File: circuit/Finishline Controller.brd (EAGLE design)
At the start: 101.6 x 53.3 mm, 20 parts, among them IC1 74HCT245N, IC2 MAX3490ESA

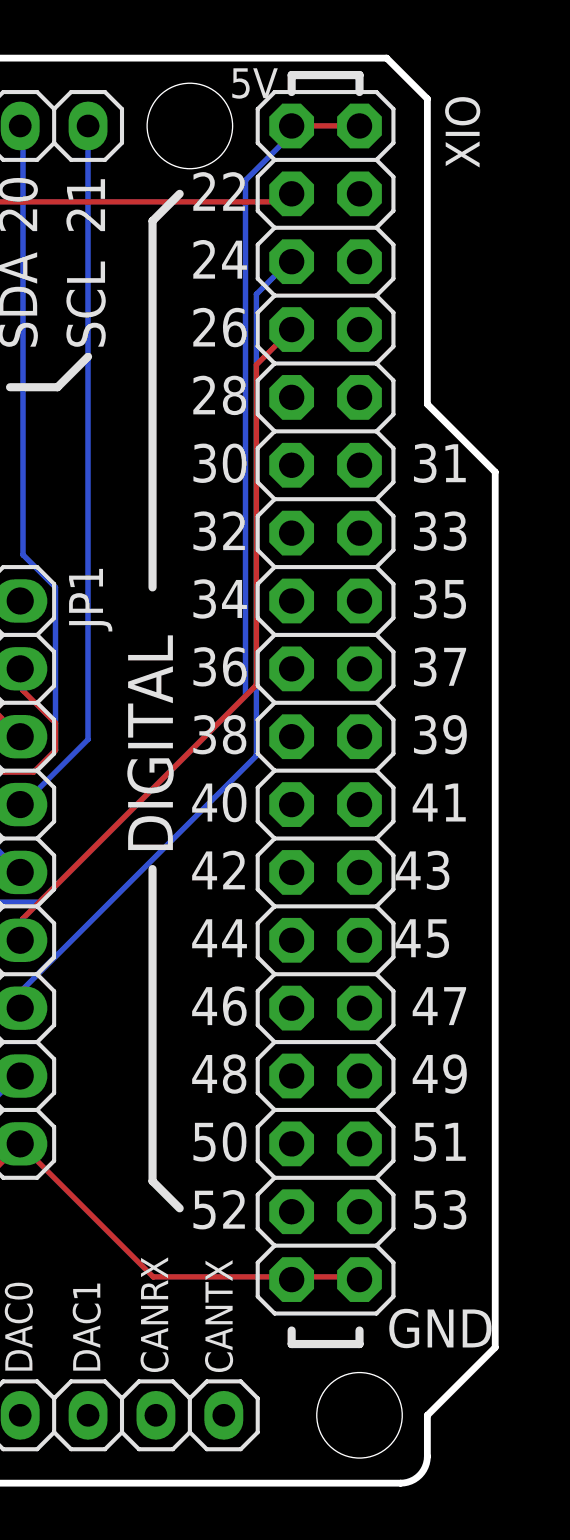
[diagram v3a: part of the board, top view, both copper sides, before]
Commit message: reduce the PCB size of the controller shield to max. 10cm
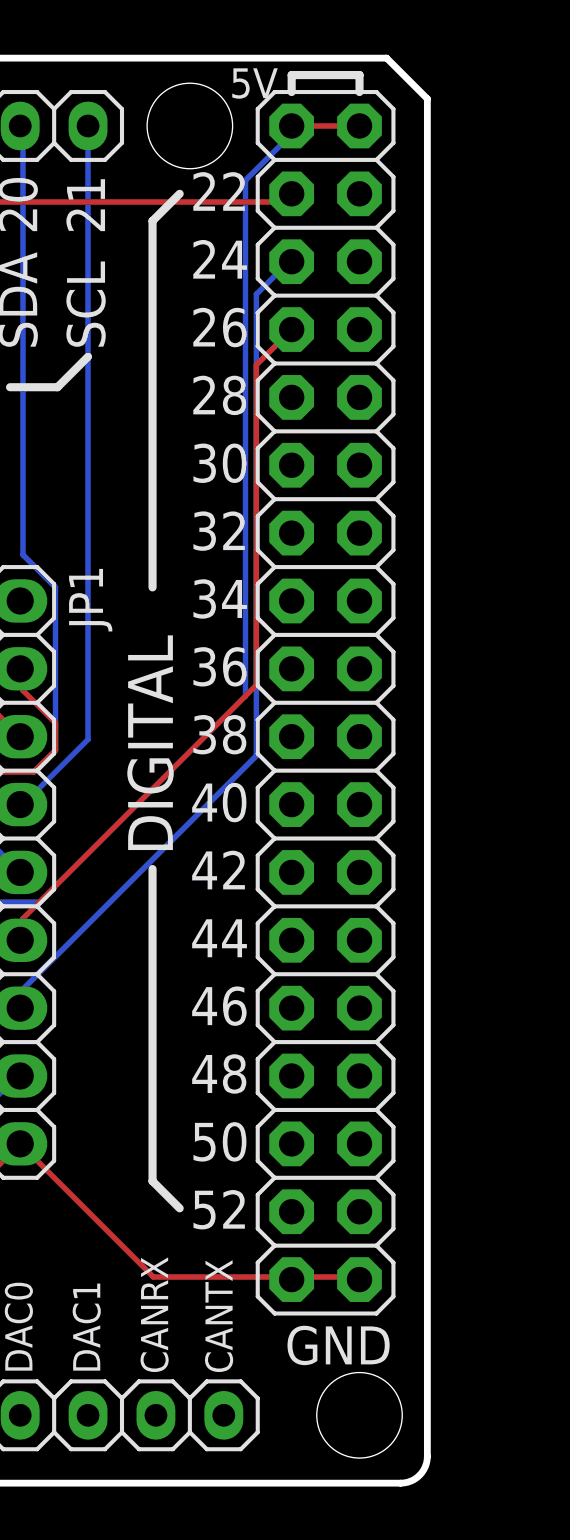
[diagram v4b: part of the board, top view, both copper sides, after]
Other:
- board size 101.6 x 53.3 mm -> 99.1 x 53.3 mm
- board text removed: "31"
- board text removed: "33"
- board text removed: "35"
- board text removed: "37"
- board text removed: "39"
- board text removed: "41"
- board text removed: "43"
- board text removed: "45"
- board text removed: "47"
- board text removed: "49"
- board text removed: "51"
- board text removed: "53"
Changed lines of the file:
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@@
 <setting verticaltext="up"/>
 </settings>
-<grid distance="0.05" unitdist="inch" unit="inch" style="lines" multiple="1" display="yes" altdistance="0.025" altunitdist="inch" altunit="inch"/>
+<grid distance="0.05" unitdist="inch" unit="mm" style="lines" multiple="1" display="yes" altdistance="0.025" altunitdist="inch" altunit="mm"/>
 <layers>
 <layer number="1" name="Top" color="4" fill="1" visible="yes" active="yes"/>
@@
 <layer number="29" name="tStop" color="2" fill="3" visible="yes" active="yes"/>
 <layer number="30" name="bStop" color="5" fill="6" visible="yes" active="yes"/>
-<layer number="31" name="tCream" color="7" fill="4" visible="yes" active="yes"/>
-<layer number="32" name="bCream" color="7" fill="5" visible="yes" active="yes"/>
-<layer number="33" name="tFinish" color="6" fill="3" visible="yes" active="yes"/>
-<layer number="34" name="bFinish" color="6" fill="6" visible="yes" active="yes"/>
+<layer number="31" name="tCream" color="7" fill="4" visible="no" active="yes"/>
+<layer number="32" name="bCream" color="7" fill="5" visible="no" active="yes"/>
+<layer number="33" name="tFinish" color="6" fill="3" visible="no" active="yes"/>
+<layer number="34" name="bFinish" color="6" fill="6" visible="no" active="yes"/>
 <layer number="35" name="tGlue" color="7" fill="4" visible="no" active="yes"/>
 <layer number="36" name="bGlue" color="7" fill="5" visible="no" active="yes"/>
@@
 <layer number="44" name="Drills" color="7" fill="1" visible="yes" active="yes"/>
 <layer number="45" name="Holes" color="7" fill="1" visible="yes" active="yes"/>
-<layer number="46" name="Milling" color="3" fill="1" visible="no" active="yes"/>
-<layer number="47" name="Measures" color="7" fill="1" visible="no" active="yes"/>
-<layer number="48" name="Document" color="7" fill="1" visible="no" active="yes"/>
+<layer number="46" name="Milling" color="3" fill="1" visible="yes" active="yes"/>
+<layer number="47" name="Measures" color="7" fill="1" visible="yes" active="yes"/>
+<layer number="48" name="Document" color="7" fill="1" visible="yes" active="yes"/>
 <layer number="49" name="ReferenceLC" color="13" fill="1" visible="yes" active="yes"/>
 <layer number="50" name="ReferenceLS" color="12" fill="1" visible="yes" active="yes"/>
@@
 <plain>
 <wire x1="97.536" y1="53.34" x2="99.06" y2="51.816" width="0.254" layer="20"/>
-<wire x1="99.06" y1="40.386" x2="101.6" y2="37.846" width="0.254" layer="20"/>
-<wire x1="101.6" y1="37.846" x2="101.6" y2="5.08" width="0.254" layer="20"/>
-<wire x1="101.6" y1="5.08" x2="99.06" y2="2.54" width="0.254" layer="20"/>
-<wire x1="99.06" y1="2.54" x2="99.06" y2="1" width="0.254" layer="20"/>
 <wire x1="99.06" y1="1" x2="98.06" y2="0" width="0.254" layer="20" curve="-90"/>
 <wire x1="98.06" y1="0" x2="1" y2="0" width="0.254" layer="20"/>
@@
 <wire x1="0" y1="52.34" x2="1" y2="53.34" width="0.254" layer="20" curve="-90"/>
 <wire x1="1" y1="53.34" x2="97.536" y2="53.34" width="0.254" layer="20"/>
-<wire x1="99.06" y1="51.816" x2="99.06" y2="40.386" width="0.254" layer="20"/>
-<wire x1="93.98" y1="5.715" x2="93.98" y2="5.207" width="0.3048" layer="21"/>
-<wire x1="93.98" y1="5.207" x2="96.52" y2="5.207" width="0.3048" layer="21"/>
-<wire x1="96.52" y1="5.207" x2="96.52" y2="5.715" width="0.3048" layer="21"/>
+<wire x1="99.06" y1="51.816" x2="99.06" y2="1" width="0.254" layer="20"/>
 <wire x1="93.98" y1="52.07" x2="93.98" y2="52.705" width="0.3048" layer="21"/>
 <wire x1="93.98" y1="52.705" x2="96.52" y2="52.705" width="0.3048" layer="21"/>
@@
 <text x="86.995" y="46.736" size="1.4224" layer="21" font="vector" ratio="12" rot="R90">21</text>
 <text x="93.472" y="52.959" size="1.1176" layer="25" font="vector" ratio="20" rot="R180">5V</text>
-<text x="97.536" y="5.08" size="1.4224" layer="25" font="vector" ratio="12">GND</text>
+<text x="93.726" y="4.445" size="1.4224" layer="25" font="vector" ratio="12">GND</text>
 <text x="90.17" y="47.625" size="1.4224" layer="21" font="vector" ratio="12">22</text>
 <text x="90.17" y="45.085" size="1.4224" layer="21" font="vector" ratio="12">24</text>
@@
 <text x="90.17" y="40.005" size="1.4224" layer="21" font="vector" ratio="12">28</text>
 <text x="90.17" y="37.465" size="1.4224" layer="21" font="vector" ratio="12">30</text>
-<text x="98.425" y="37.465" size="1.4224" layer="21" font="vector" ratio="12">31</text>
 <text x="90.17" y="34.925" size="1.4224" layer="21" font="vector" ratio="12">32</text>
-<text x="98.425" y="34.925" size="1.4224" layer="21" font="vector" ratio="12">33</text>
 <text x="90.17" y="32.385" size="1.4224" layer="21" font="vector" ratio="12">34</text>
-<text x="98.425" y="32.385" size="1.4224" layer="21" font="vector" ratio="12">35</text>
 <text x="90.17" y="29.845" size="1.4224" layer="21" font="vector" ratio="12">36</text>
-<text x="98.425" y="29.845" size="1.4224" layer="21" font="vector" ratio="12">37</text>
 <text x="90.17" y="27.305" size="1.4224" layer="21" font="vector" ratio="12">38</text>
-<text x="98.425" y="27.305" size="1.4224" layer="21" font="vector" ratio="12">39</text>
-<text x="98.425" y="24.765" size="1.4224" layer="21" font="vector" ratio="12">41</text>
 <text x="90.17" y="24.765" size="1.4224" layer="21" font="vector" ratio="12">40</text>
-<text x="97.79" y="22.225" size="1.4224" layer="21" font="vector" ratio="12">43</text>
 <text x="90.17" y="22.225" size="1.4224" layer="21" font="vector" ratio="12">42</text>
-<text x="97.79" y="19.685" size="1.4224" layer="21" font="vector" ratio="12">45</text>
-<text x="98.425" y="17.145" size="1.4224" layer="21" font="vector" ratio="12">47</text>
-<text x="98.425" y="14.605" size="1.4224" layer="21" font="vector" ratio="12">49</text>
-<text x="98.425" y="12.065" size="1.4224" layer="21" font="vector" ratio="12">51</text>
 <text x="90.17" y="19.685" size="1.4224" layer="21" font="vector" ratio="12">44</text>
 <text x="90.17" y="17.145" size="1.4224" layer="21" font="vector" ratio="12">46</text>
 <text x="90.17" y="12.065" size="1.4224" layer="21" font="vector" ratio="12">50</text>
 <text x="90.17" y="14.605" size="1.4224" layer="21" font="vector" ratio="12">48</text>
-<text x="98.425" y="9.525" size="1.4224" layer="21" font="vector" ratio="12">53</text>
 <text x="90.17" y="9.525" size="1.4224" layer="21" font="vector" ratio="12">52</text>
 <text x="89.535" y="23.495" size="1.6764" layer="25" font="vector" ratio="15" rot="R90">DIGITAL</text>
@@
 </element>
 <element name="XIO" library="SmartPrj" package="2X18" value="18x2F-H8.5" x="95.25" y="29.21" locked="yes" smashed="yes" rot="R270">
-<attribute name="NAME" x="99.7458" y="51.9684" size="1.27" layer="25" ratio="10" rot="R270"/>
 <attribute name="VALUE" x="90.805" y="52.07" size="1.27" layer="27" rot="R270"/>
 </element>

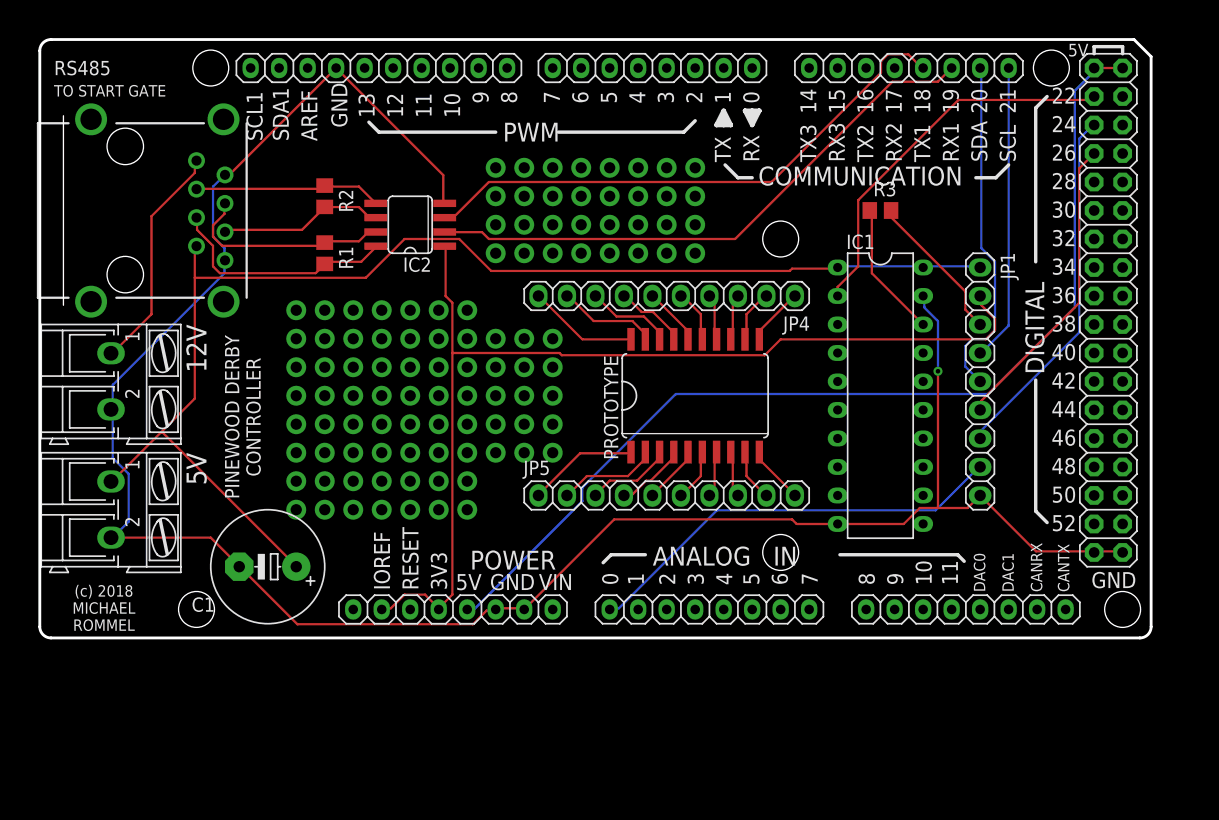
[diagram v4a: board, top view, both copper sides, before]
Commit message: change the pin assignment for LDR and WS2812DATA
This uses a high power pin for the LED data and a normal analog pin for
the LDR line.
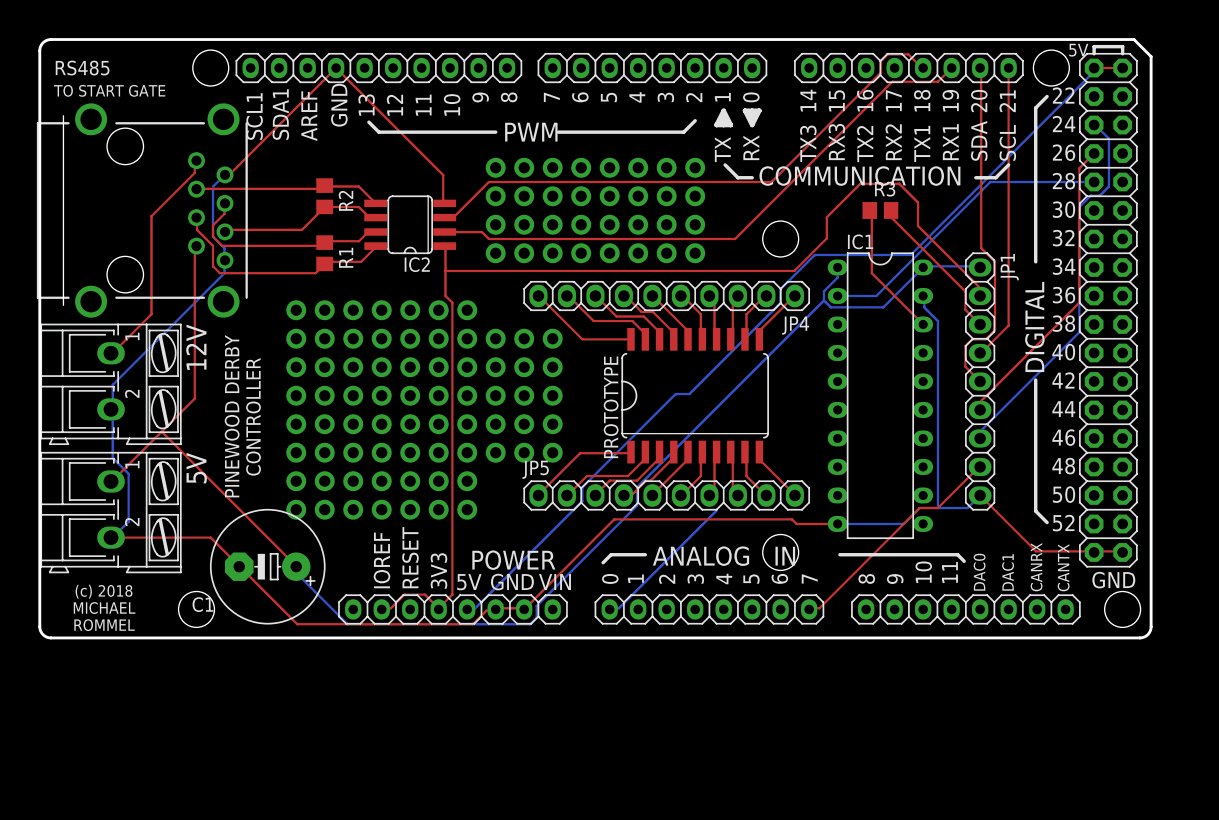
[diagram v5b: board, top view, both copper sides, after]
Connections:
- net AD0: no longer JP1.8
- net AD7: now also JP1.8
- net PIN22: no longer IC1.2
- net PIN28: now also IC1.2
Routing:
- net PIN22: track 34.2 -> 0.00 mm
- net PIN28: track 0.00 -> 27.1 mm
- net AD0: track 38.3 -> 13.3 mm
- net AD7: track 0.00 -> 20.6 mm
- net +5V: track 90.7 -> 80.1 mm
- net +5VEXT: track 114.2 -> 123.4 mm
- net +3.3V: track 92.4 -> 97.2 mm
- net PIN24: track 32.2 -> 33.8 mm
- net GND: vias 1 -> 0

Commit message: correct some schematics mistakes and add gerber files
A demo mode button was added to the controller, the layout of the
controller shield as well as the startgate displays were changed.
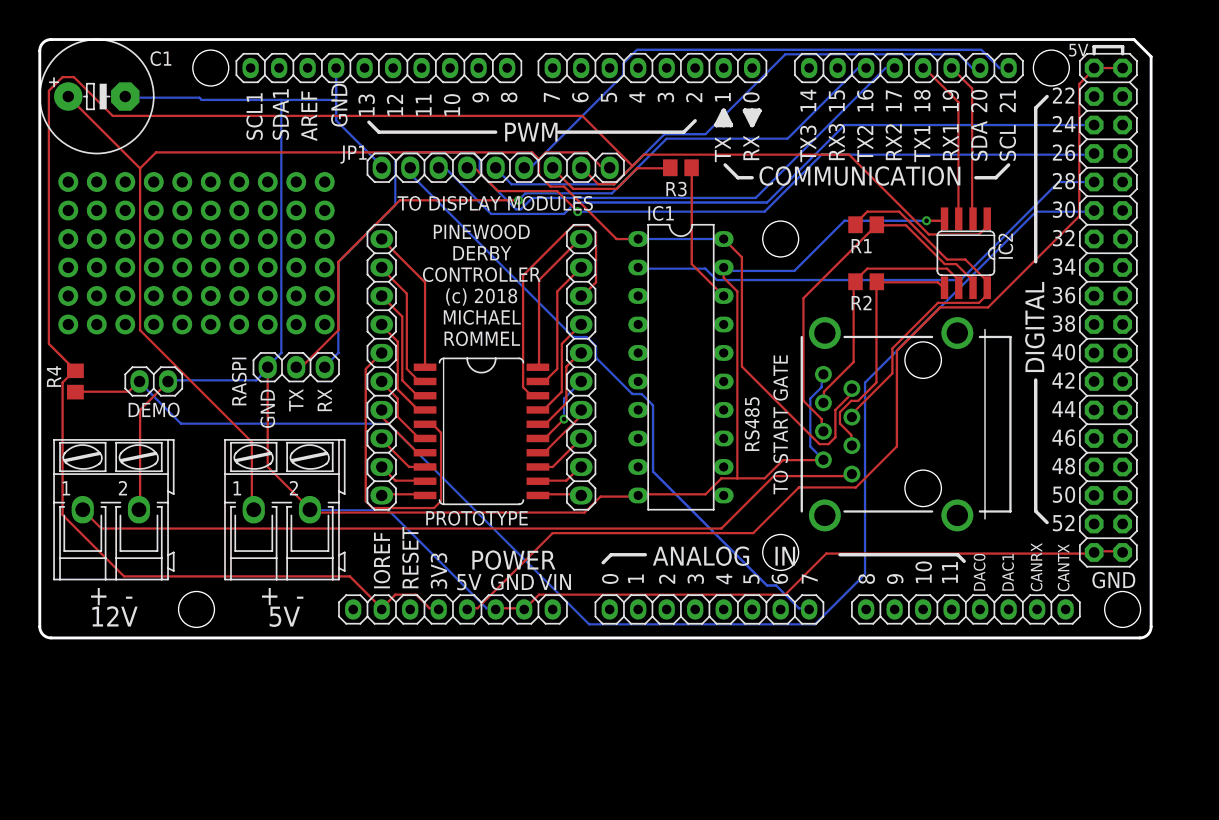
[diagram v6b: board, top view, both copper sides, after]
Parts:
- added JP2: DEMO, pinhead:1X02
- added JP3: RASPI, pinhead:1X03
- added R4: 10K, resistor:R0805
- moved RS485 73.6 mm to (78.7, 19.1), turned to 90 degrees
- moved IC2 49.6 mm to (82.5, 34.3), turned to 180 degrees
- moved R2 48.9 mm to (73.7, 31.8), turned to 180 degrees
- moved R1 48.3 mm to (73.7, 36.8), turned to 180 degrees
- moved JP1 47.2 mm to (40.6, 41.9), turned to 180 degrees
- moved C1 44.6 mm to (5.08, 48.3), turned to 0 degrees
- moved JP5 27.9 mm to (30.5, 24.1), turned to 270 degrees
- moved PROTOTYPE 19.3 mm to (39.4, 18.4), turned to 270 degrees
- moved R3 18.2 mm to (57.1, 41.9), turned to 180 degrees
- moved IC1 18.0 mm to (57.1, 24.1)
- moved 5V 15.2 mm to (21.6, 11.4), turned to 0 degrees
- moved 12V 11.4 mm to (6.35, 11.4), turned to 0 degrees
- moved JP4 9.92 mm to (48.3, 24.1), turned to 90 degrees
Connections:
- removed net +3.3V: IC2.1, JP1.2, POWER.2, POWER.4
- new net +3V3: IC2.1, JP1.2, POWER.2, POWER.4, R4.2
- net GND: now also JP2.2, JP3.3
- net PIN30: now also JP2.1, R4.1
- net RX2: now also JP3.1
- net TX2: now also JP3.2
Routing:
- net +3V3: track 0.00 -> 175.1 mm
- net PIN30: track 0.00 -> 125.4 mm
- net +3.3V: track 97.2 -> 0.00 mm
- net GND: track 189.2 -> 266.1 mm, vias 0 -> 1
- net RX2: track 0.00 -> 73.8 mm
- net TX2: track 0.00 -> 65.4 mm, vias 0 -> 1
- net +12VEXT: track 20.4 -> 71.3 mm
- net RX1: track 51.8 -> 14.2 mm
- net AD7: track 20.6 -> 56.3 mm
- net TX1: track 49.8 -> 14.8 mm
- net PIN26: track 27.1 -> 59.6 mm, vias 0 -> 1
- net PIN24: track 33.8 -> 63.4 mm
- net N$82: track 5.16 -> 28.9 mm
- net SCL0: track 26.5 -> 48.8 mm
- net N$89: track 7.79 -> 26.5 mm
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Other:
- board text added: "+ -"
- board text added: "DEMO"
- board text added: "PINEWOOD DERBY CONTROLLER (c) 2018 MICHAEL ROMMEL"
- board text added: "RASPI"
- board text added: "TO DISPLAY MODULES"
- board text removed: "(c) 2018 MICHAEL ROMMEL"
- board text removed: "PINEWOOD DERBY CONTROLLER"
